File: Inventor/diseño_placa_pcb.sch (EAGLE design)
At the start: 11 parts, among them IC2 7805T

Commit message: otro diseño pcb
diseño considerando 1.2 mm
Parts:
- IC2: value 7805T -> 7805TV; device linear:7805T -> linear:7805TV
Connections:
- net N$22: now also U$1.GND@1; no longer U$1.GND@2
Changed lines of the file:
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@@
 <grid distance="0.1" unitdist="inch" unit="inch" style="lines" multiple="1" display="no" altdistance="0.01" altunitdist="inch" altunit="inch"/>
 <layers>
-<layer number="1" name="Top" color="4" fill="1" visible="no" active="no"/>
-<layer number="16" name="Bottom" color="1" fill="1" visible="no" active="no"/>
-<layer number="17" name="Pads" color="2" fill="1" visible="no" active="no"/>
-<layer number="18" name="Vias" color="2" fill="1" visible="no" active="no"/>
-<layer number="19" name="Unrouted" color="6" fill="1" visible="no" active="no"/>
-<layer number="20" name="Dimension" color="24" fill="1" visible="no" active="no"/>
-<layer number="21" name="tPlace" color="7" fill="1" visible="no" active="no"/>
-<layer number="22" name="bPlace" color="7" fill="1" visible="no" active="no"/>
-<layer number="23" name="tOrigins" color="15" fill="1" visible="no" active="no"/>
-<layer number="24" name="bOrigins" color="15" fill="1" visible="no" active="no"/>
-<layer number="25" name="tNames" color="7" fill="1" visible="no" active="no"/>
-<layer number="26" name="bNames" color="7" fill="1" visible="no" active="no"/>
-<layer number="27" name="tValues" color="7" fill="1" visible="no" active="no"/>
-<layer number="28" name="bValues" color="7" fill="1" visible="no" active="no"/>
+<layer number="1" name="Top" color="4" fill="1" visible="yes" active="no"/>
+<layer number="16" name="Bottom" color="1" fill="1" visible="yes" active="no"/>
+<layer number="17" name="Pads" color="2" fill="1" visible="yes" active="no"/>
+<layer number="18" name="Vias" color="2" fill="1" visible="yes" active="no"/>
+<layer number="19" name="Unrouted" color="6" fill="1" visible="yes" active="no"/>
+<layer number="20" name="Dimension" color="24" fill="1" visible="yes" active="no"/>
+<layer number="21" name="tPlace" color="7" fill="1" visible="yes" active="no"/>
+<layer number="22" name="bPlace" color="7" fill="1" visible="yes" active="no"/>
+<layer number="23" name="tOrigins" color="15" fill="1" visible="yes" active="no"/>
+<layer number="24" name="bOrigins" color="15" fill="1" visible="yes" active="no"/>
+<layer number="25" name="tNames" color="7" fill="1" visible="yes" active="no"/>
+<layer number="26" name="bNames" color="7" fill="1" visible="yes" active="no"/>
+<layer number="27" name="tValues" color="7" fill="1" visible="yes" active="no"/>
+<layer number="28" name="bValues" color="7" fill="1" visible="yes" active="no"/>
 <layer number="29" name="tStop" color="7" fill="3" visible="no" active="no"/>
 <layer number="30" name="bStop" color="7" fill="6" visible="no" active="no"/>
@@
 <layer number="35" name="tGlue" color="7" fill="4" visible="no" active="no"/>
 <layer number="36" name="bGlue" color="7" fill="5" visible="no" active="no"/>
-<layer number="37" name="tTest" color="7" fill="1" visible="no" active="no"/>
-<layer number="38" name="bTest" color="7" fill="1" visible="no" active="no"/>
+<layer number="37" name="tTest" color="7" fill="1" visible="yes" active="no"/>
+<layer number="38" name="bTest" color="7" fill="1" visible="yes" active="no"/>
 <layer number="39" name="tKeepout" color="4" fill="11" visible="no" active="no"/>
 <layer number="40" name="bKeepout" color="1" fill="11" visible="no" active="no"/>
@@
 <layer number="44" name="Drills" color="7" fill="1" visible="no" active="no"/>
 <layer number="45" name="Holes" color="7" fill="1" visible="no" active="no"/>
-<layer number="46" name="Milling" color="3" fill="1" visible="no" active="no"/>
-<layer number="47" name="Measures" color="7" fill="1" visible="no" active="no"/>
-<layer number="48" name="Document" color="7" fill="1" visible="no" active="no"/>
-<layer number="49" name="Reference" color="7" fill="1" visible="no" active="no"/>
-<layer number="50" name="dxf" color="7" fill="1" visible="no" active="no"/>
-<layer number="51" name="tDocu" color="7" fill="1" visible="no" active="no"/>
-<layer number="52" name="bDocu" color="7" fill="1" visible="no" active="no"/>
-<layer number="53" name="tGND_GNDA" color="7" fill="1" visible="no" active="no"/>
-<layer number="54" name="bGND_GNDA" color="7" fill="1" visible="no" active="no"/>
-<layer number="56" name="wert" color="7" fill="1" visible="no" active="no"/>
+<layer number="46" name="Milling" color="3" fill="1" visible="yes" active="no"/>
+<layer number="47" name="Measures" color="7" fill="1" visible="yes" active="no"/>
+<layer number="48" name="Document" color="7" fill="1" visible="yes" active="no"/>
+<layer number="49" name="Reference" color="7" fill="1" visible="yes" active="no"/>
+<layer number="50" name="dxf" color="7" fill="1" visible="yes" active="no"/>
+<layer number="51" name="tDocu" color="7" fill="1" visible="yes" active="no"/>
+<layer number="52" name="bDocu" color="7" fill="1" visible="yes" active="no"/>
+<layer number="53" name="tGND_GNDA" color="7" fill="1" visible="yes" active="no"/>
+<layer number="54" name="bGND_GNDA" color="7" fill="1" visible="yes" active="no"/>
+<layer number="56" name="wert" color="7" fill="1" visible="yes" active="no"/>
 <layer number="88" name="SimResults" color="9" fill="1" visible="yes" active="yes"/>
 <layer number="89" name="SimProbes" color="9" fill="1" visible="yes" active="yes"/>
@@
 <part name="X3" library="con-wago-500" library_urn="urn:adsk.eagle:library:195" deviceset="W237-102" device="" package3d_urn="urn:adsk.eagle:package:10688/1"/>
 <part name="X4" library="con-wago-500" library_urn="urn:adsk.eagle:library:195" deviceset="W237-102" device="" package3d_urn="urn:adsk.eagle:package:10688/1"/>
-<part name="IC2" library="linear" library_urn="urn:adsk.eagle:library:262" deviceset="78*" device="T" package3d_urn="urn:adsk.eagle:package:16414/1" technology="05"/>
+<part name="IC2" library="linear" library_urn="urn:adsk.eagle:library:262" deviceset="78*" device="TV" package3d_urn="urn:adsk.eagle:package:16417/2" technology="05" value="7805TV"/>
 <part name="VCC1" library="con-wago-500" library_urn="urn:adsk.eagle:library:195" deviceset="W237-102" device="" package3d_urn="urn:adsk.eagle:package:10688/1"/>
 <part name="U$2" library="HR911105A" deviceset="HR911105A" device=""/>
@@
 <wire x1="111.76" y1="124.46" x2="132.08" y2="124.46" width="0.1524" layer="91"/>
 <wire x1="132.08" y1="124.46" x2="132.08" y2="114.3" width="0.1524" layer="91"/>
-<wire x1="127" y1="114.3" x2="127" y2="58.42" width="0.1524" layer="91"/>
-<pinref part="U$1" gate="G$1" pin="GND@2"/>
-<wire x1="127" y1="58.42" x2="104.14" y2="58.42" width="0.1524" layer="91"/>
-</segment>
-</net>
+<wire x1="127" y1="114.3" x2="127" y2="60.96" width="0.1524" layer="91"/>
+<pinref part="U$1" gate="G$1" pin="GND@1"/>
+<wire x1="127" y1="60.96" x2="127" y2="58.42" width="0.1524" layer="91"/>
+<wire x1="68.58" y1="58.42" x2="68.58" y2="50.8" width="0.1524" layer="91"/>
+<wire x1="68.58" y1="50.8" x2="127" y2="50.8" width="0.1524" layer="91"/>
+<wire x1="127" y1="50.8" x2="127" y2="58.42" width="0.1524" layer="91"/>
+</segment>
+</net>

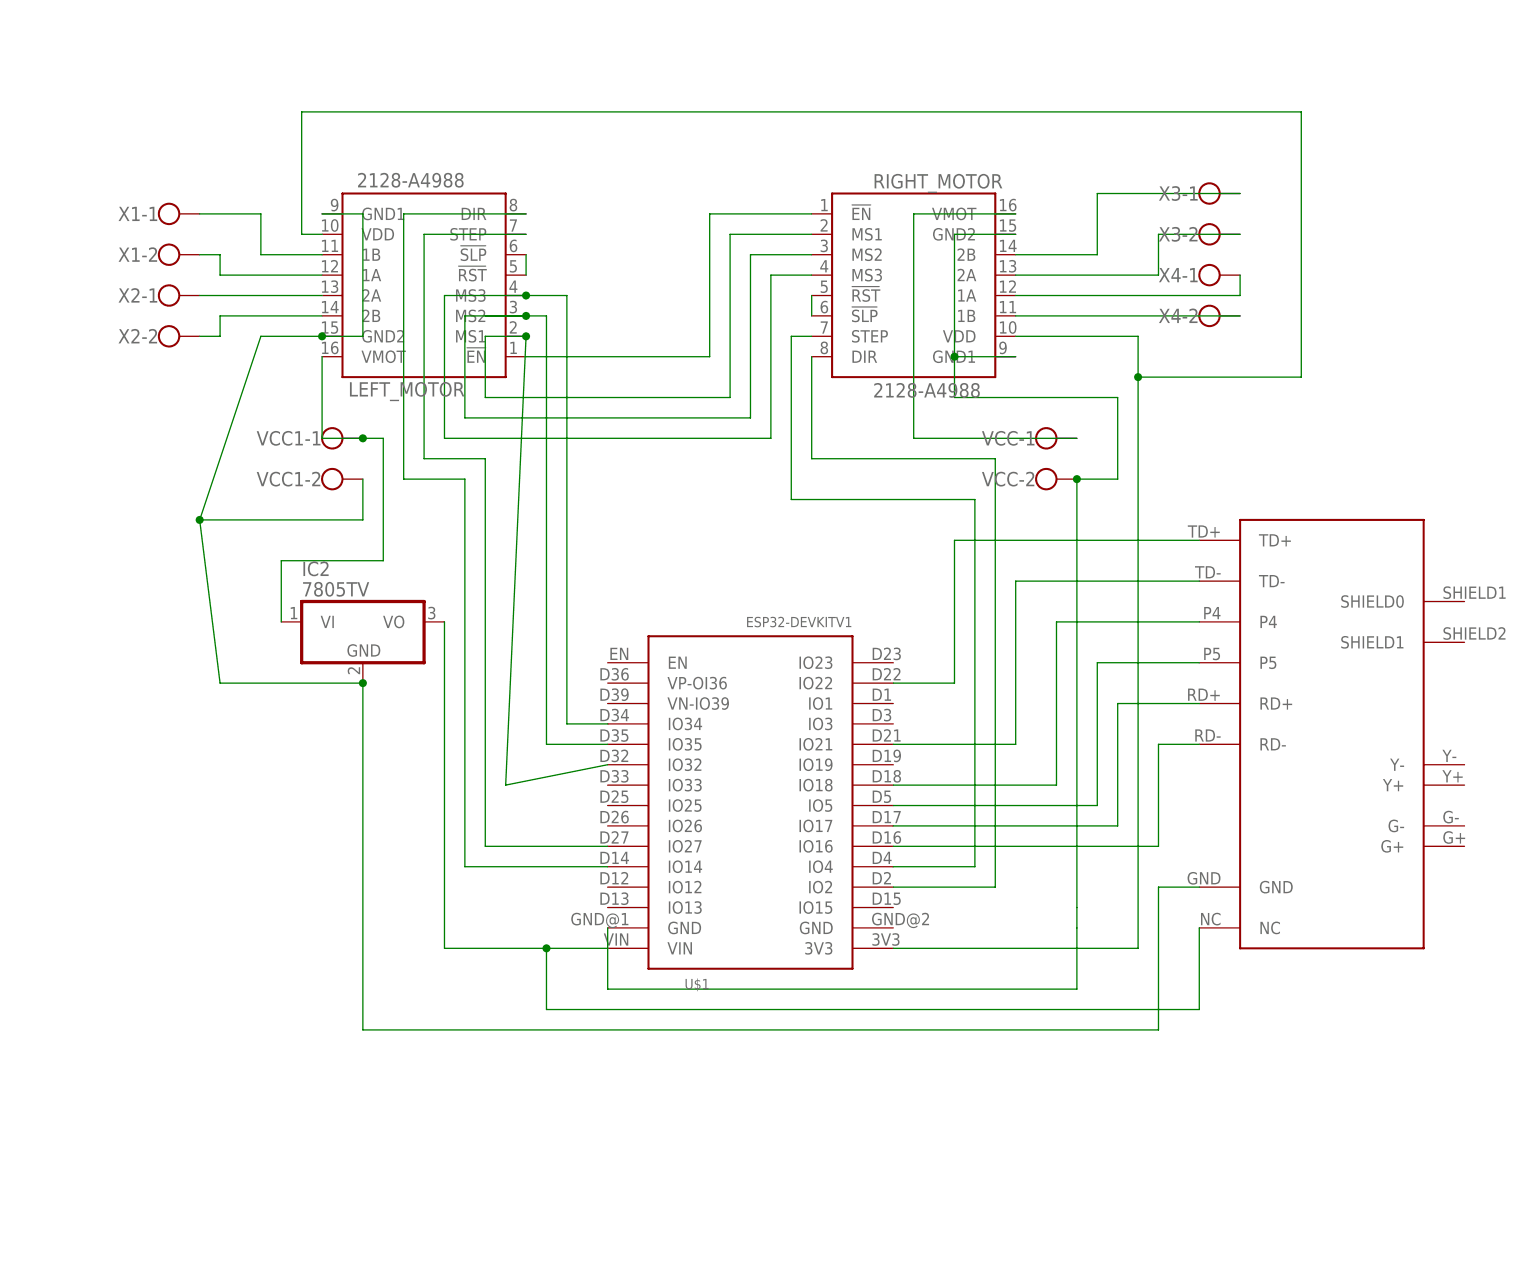
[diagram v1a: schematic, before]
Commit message: diseño pcb
se realizó el diseño PCB considerando pistas de 1 mm
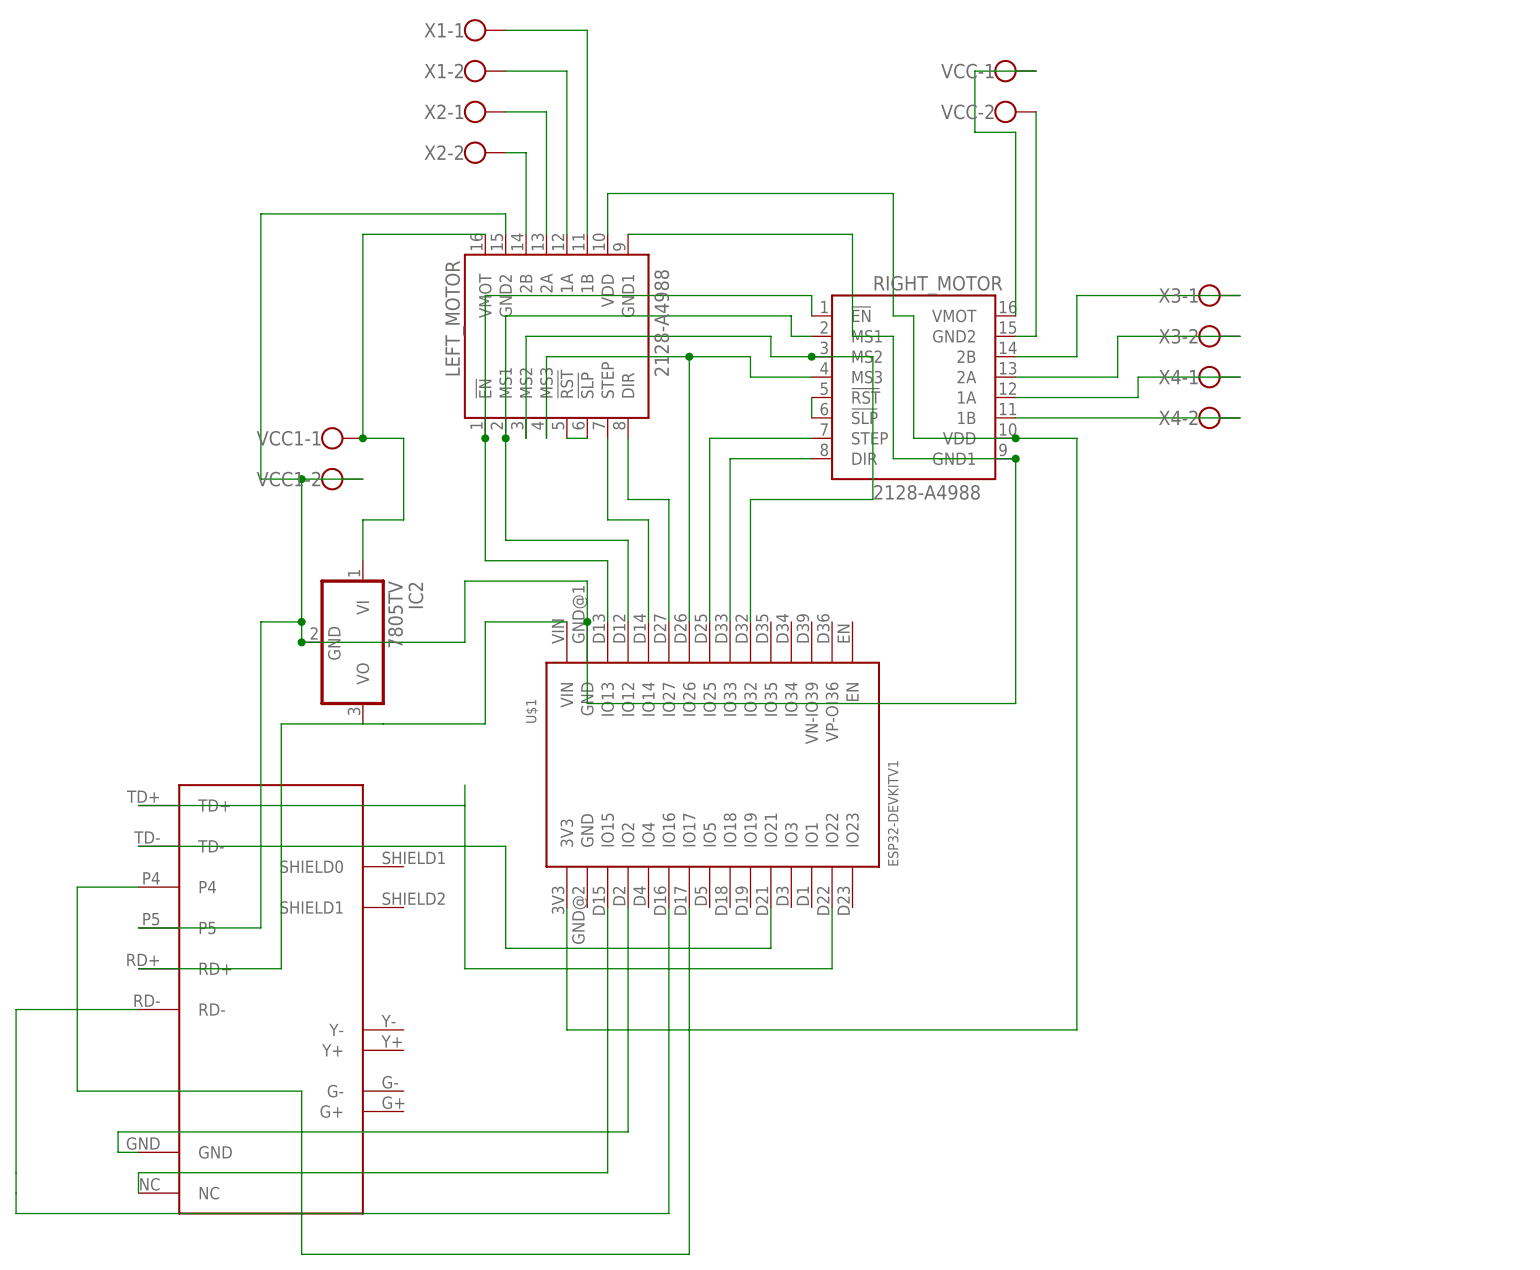
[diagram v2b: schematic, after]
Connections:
- removed net N$20 (its old number): LEFT_MOTOR.DIR, U$1.IO14
- removed net N$22 (its old number): RIGHT_MOTOR.GND1, RIGHT_MOTOR.GND2, U$1.GND@1, VCC-2.KL
- removed net N$24: IC2.GND, LEFT_MOTOR.GND1, LEFT_MOTOR.GND2, U$2.GND, VCC1-2.KL
- removed net N$25 (its old number): U$1.IO17, U$2.RD+
- removed net N$26 (its old number): U$1.IO5, U$2.P5
- removed net N$27: LEFT_MOTOR.MS2, RIGHT_MOTOR.MS2, U$1.IO35
- removed net N$28 (its old number): U$1.IO18, U$2.P4
- removed net N$6 (its old number): RIGHT_MOTOR.DIR, U$1.IO2
- new net N$10: RIGHT_MOTOR.STEP, U$1.IO25
- new net N$11: RIGHT_MOTOR.DIR, U$1.IO33
- new net N$2: LEFT_MOTOR.MS1, RIGHT_MOTOR.MS1, U$1.IO12
- new net N$3: LEFT_MOTOR.MS2, RIGHT_MOTOR.MS2, U$1.IO32
- new net N$30: U$1.IO17, U$2.P4
- new net N$31: U$1.IO2, U$2.GND
- new net N$32: U$1.IO15, U$2.NC
- new net N$5: LEFT_MOTOR.MS3, RIGHT_MOTOR.MS3, U$1.IO26
- net N$1: now also LEFT_MOTOR.!EN, RIGHT_MOTOR.!EN, U$1.IO13; no longer LEFT_MOTOR.MS3, RIGHT_MOTOR.MS3, U$1.IO34
- net N$12: now also IC2.GND, LEFT_MOTOR.GND1, LEFT_MOTOR.GND2, RIGHT_MOTOR.GND1, U$1.GND@1, U$2.P5, VCC1-2.KL; no longer LEFT_MOTOR.!EN, RIGHT_MOTOR.!EN
- net N$13: now also U$2.RD+; no longer U$2.NC
- net N$14: now also RIGHT_MOTOR.GND2, VCC-2.KL; no longer LEFT_MOTOR.STEP, U$1.IO27
- net N$7: now also LEFT_MOTOR.STEP, U$1.IO14; no longer LEFT_MOTOR.MS1, RIGHT_MOTOR.MS1, U$1.IO32
- net N$9: now also LEFT_MOTOR.DIR, U$1.IO27; no longer RIGHT_MOTOR.STEP, U$1.IO4
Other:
- moved on the sheet: IC2, LEFT_MOTOR, RIGHT_MOTOR, U$1, VCC-1, VCC-2, X1-1, X1-2, X2-1, X2-2, X3-1, X3-2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

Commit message: se crearon clases
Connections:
- net N$1 renamed ENABLE
- net N$10 renamed STEP_Y
- net N$11 renamed DIR_Y
- net N$12 renamed GND
- net N$13 renamed VCC_5V
- net N$15 renamed VCC_3.3
- net N$2 renamed MS1
- net N$25 renamed RX
- net N$26 renamed VIN
- net N$3 renamed MS2
- net N$30 renamed TX
- net N$31 renamed RDY1
- net N$32 renamed VBB_EN1
- net N$5 renamed MS3
- net N$7 renamed STEP_X
- net N$9 renamed DIR_X
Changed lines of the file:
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@@
 </segment>
 </net>
-<net name="N$1" class="0">
+<net name="ENABLE" class="0">
 <segment>
 <pinref part="LEFT_MOTOR" gate="G$1" pin="!EN"/>
@@
 </segment>
 </net>
-<net name="N$2" class="0">
+<net name="MS1" class="0">
 <segment>
 <pinref part="LEFT_MOTOR" gate="G$1" pin="MS1"/>
@@
 </segment>
 </net>
-<net name="N$3" class="0">
+<net name="MS2" class="0">
 <segment>
 <pinref part="LEFT_MOTOR" gate="G$1" pin="MS2"/>
@@
 </segment>
 </net>
-<net name="N$5" class="0">
+<net name="MS3" class="0">
 <segment>
 <pinref part="LEFT_MOTOR" gate="G$1" pin="MS3"/>
@@
 </segment>
 </net>
-<net name="N$7" class="0">
+<net name="STEP_X" class="0">
 <segment>
 <pinref part="LEFT_MOTOR" gate="G$1" pin="STEP"/>
@@
 </segment>
 </net>
-<net name="N$9" class="0">
+<net name="DIR_X" class="0">
 <segment>
 <pinref part="LEFT_MOTOR" gate="G$1" pin="DIR"/>
@@
 </segment>
 </net>
-<net name="N$10" class="0">
+<net name="STEP_Y" class="0">
 <segment>
 <pinref part="U$1" gate="G$1" pin="IO25"/>
@@
 </segment>
 </net>
-<net name="N$11" class="0">
+<net name="DIR_Y" class="0">
 <segment>
 <pinref part="RIGHT_MOTOR" gate="G$1" pin="DIR"/>
@@
 </segment>
 </net>
-<net name="N$12" class="0">
+<net name="GND" class="0">
 <segment>
 <pinref part="U$1" gate="G$1" pin="GND@1"/>
@@
 </segment>
 </net>
-<net name="N$13" class="0">
+<net name="VCC_5V" class="0">
 <segment>
 <pinref part="IC2" gate="A1" pin="VO"/>
@@
 </segment>
 </net>
-<net name="N$15" class="0">
+<net name="VCC_3.3" class="0">
 <segment>
 <pinref part="U$1" gate="G$1" pin="3V3"/>
@@
 </segment>
 </net>
-<net name="N$26" class="0">
+<net name="VIN" class="0">
 <segment>
 <pinref part="IC2" gate="A1" pin="VI"/>
@@
 </segment>
 </net>
-<net name="N$30" class="0">
+<net name="TX" class="0">
 <segment>
 <pinref part="U$2" gate="G$1" pin="P4"/>
@@
 </segment>
 </net>
-<net name="N$25" class="0">
+<net name="RX" class="0">
 <segment>
 <pinref part="U$1" gate="G$1" pin="IO16"/>
@@
 </segment>
 </net>
-<net name="N$31" class="0">
+<net name="RDY1" class="0">
 <segment>
 <pinref part="U$2" gate="G$1" pin="GND"/>
@@
 </segment>
 </net>
-<net name="N$32" class="0">
+<net name="VBB_EN1" class="0">
 <segment>
 <pinref part="U$2" gate="G$1" pin="NC"/>
